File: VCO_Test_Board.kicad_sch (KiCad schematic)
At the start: 19 parts, among them J1 PCB.SMAFRA.HT, J2 PCB.SMAFRA.HT, J3 Tune Voltage Input, J4 VCC, Y1 MAX2607EUT+T

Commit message: Export gerber files.
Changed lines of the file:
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@@
   (junction (at 177.8 88.9) (diameter 0) (color 0 0 0 0)
   )
+  (junction (at 158.75 118.11) (diameter 0) (color 0 0 0 0)
+  )
+  (junction (at 135.89 59.69) (diameter 0) (color 0 0 0 0)
+  )
   (junction (at 175.26 88.9) (diameter 0) (color 0 0 0 0)
   )
@@
   (junction (at 130.81 88.9) (diameter 0) (color 0 0 0 0)
   )
+  (junction (at 147.32 64.77) (diameter 0) (color 0 0 0 0)
+  )
   (junction (at 130.81 86.36) (diameter 0) (color 0 0 0 0)
   )
-  (junction (at 162.56 118.11) (diameter 0) (color 0 0 0 0)
-  )
-  (junction (at 132.08 59.69) (diameter 0) (color 0 0 0 0)
+  (junction (at 135.89 120.65) (diameter 0) (color 0 0 0 0)
   )
   (junction (at 138.43 78.74) (diameter 0) (color 0 0 0 0)
@@
   (junction (at 170.18 91.44) (diameter 0) (color 0 0 0 0)
   )
-  (junction (at 147.32 129.54) (diameter 0) (color 0 0 0 0)
-  )
-  (junction (at 132.08 120.65) (diameter 0) (color 0 0 0 0)
-  )
   (junction (at 138.43 86.36) (diameter 0) (color 0 0 0 0)
   )
-  (junction (at 162.56 57.15) (diameter 0) (color 0 0 0 0)
+  (junction (at 147.32 125.73) (diameter 0) (color 0 0 0 0)
+  )
+  (junction (at 158.75 57.15) (diameter 0) (color 0 0 0 0)
   )
   (junction (at 167.64 86.36) (diameter 0) (color 0 0 0 0)
@@
   (junction (at 119.38 88.9) (diameter 0) (color 0 0 0 0)
   )
-  (junction (at 147.32 68.58) (diameter 0) (color 0 0 0 0)
-  )
   (junction (at 96.52 88.9) (diameter 0) (color 0 0 0 0)
   )
@@
     (stroke (width 0) (type default))
   )
-  (wire (pts (xy 132.08 120.65) (xy 137.16 120.65))
-    (stroke (width 0) (type default))
-  )
-  (wire (pts (xy 147.32 68.58) (xy 162.56 68.58))
+  (wire (pts (xy 147.32 64.77) (xy 158.75 64.77))
     (stroke (width 0) (type default))
   )
@@
     (stroke (width 0) (type default))
   )
-  (wire (pts (xy 132.08 118.11) (xy 137.16 118.11))
+  (wire (pts (xy 135.89 118.11) (xy 137.16 118.11))
     (stroke (width 0) (type default))
   )
@@
     (stroke (width 0) (type default))
   )
-  (wire (pts (xy 157.48 54.61) (xy 162.56 54.61))
+  (wire (pts (xy 147.32 125.73) (xy 147.32 127))
+    (stroke (width 0) (type default))
+  )
+  (wire (pts (xy 157.48 54.61) (xy 158.75 54.61))
     (stroke (width 0) (type default))
   )
@@
     (stroke (width 0) (type default))
   )
-  (wire (pts (xy 147.32 134.62) (xy 147.32 129.54))
-    (stroke (width 0) (type default))
-  )
   (wire (pts (xy 115.57 88.9) (xy 119.38 88.9))
     (stroke (width 0) (type default))
@@
     (stroke (width 0) (type default))
   )
-  (wire (pts (xy 157.48 57.15) (xy 162.56 57.15))
+  (wire (pts (xy 157.48 57.15) (xy 158.75 57.15))
     (stroke (width 0) (type default))
   )
@@
     (stroke (width 0) (type default))
   )
-  (wire (pts (xy 132.08 129.54) (xy 147.32 129.54))
+  (wire (pts (xy 135.89 125.73) (xy 147.32 125.73))
     (stroke (width 0) (type default))
   )
@@
     (stroke (width 0) (type default))
   )
-  (wire (pts (xy 157.48 115.57) (xy 162.56 115.57))
-    (stroke (width 0) (type default))
-  )
-  (wire (pts (xy 132.08 59.69) (xy 137.16 59.69))
-    (stroke (width 0) (type default))
-  )
-  (wire (pts (xy 132.08 120.65) (xy 132.08 118.11))
-    (stroke (width 0) (type default))
-  )
-  (wire (pts (xy 162.56 57.15) (xy 162.56 68.58))
+  (wire (pts (xy 157.48 115.57) (xy 158.75 115.57))
+    (stroke (width 0) (type default))
+  )
+  (wire (pts (xy 135.89 120.65) (xy 135.89 118.11))
+    (stroke (width 0) (type default))
+  )
+  (wire (pts (xy 158.75 57.15) (xy 158.75 64.77))
     (stroke (width 0) (type default))
   )
@@
     (stroke (width 0) (type default))
   )
-  (wire (pts (xy 147.32 69.85) (xy 147.32 68.58))
-    (stroke (width 0) (type default))
-  )
   (wire (pts (xy 175.26 86.36) (xy 175.26 88.9))
     (stroke (width 0) (type default))
   )
-  (wire (pts (xy 162.56 54.61) (xy 162.56 57.15))
-    (stroke (width 0) (type default))
-  )
-  (wire (pts (xy 162.56 115.57) (xy 162.56 118.11))
+  (wire (pts (xy 158.75 54.61) (xy 158.75 57.15))
+    (stroke (width 0) (type default))
+  )
+  (wire (pts (xy 158.75 115.57) (xy 158.75 118.11))
     (stroke (width 0) (type default))
   )
@@
     (stroke (width 0) (type default))
   )
-  (wire (pts (xy 132.08 129.54) (xy 132.08 120.65))
-    (stroke (width 0) (type default))
-  )
-  (wire (pts (xy 132.08 59.69) (xy 132.08 57.15))
-    (stroke (width 0) (type default))
-  )
-  (wire (pts (xy 132.08 57.15) (xy 137.16 57.15))
-    (stroke (width 0) (type default))
-  )
-  (wire (pts (xy 157.48 118.11) (xy 162.56 118.11))
-    (stroke (width 0) (type default))
-  )
-  (wire (pts (xy 132.08 68.58) (xy 147.32 68.58))
-    (stroke (width 0) (type default))
-  )
-  (wire (pts (xy 162.56 118.11) (xy 162.56 129.54))
+  (wire (pts (xy 147.32 64.77) (xy 147.32 66.04))
+    (stroke (width 0) (type default))
+  )
+  (wire (pts (xy 135.89 125.73) (xy 135.89 120.65))
+    (stroke (width 0) (type default))
+  )
+  (wire (pts (xy 135.89 59.69) (xy 135.89 57.15))
+    (stroke (width 0) (type default))
+  )
+  (wire (pts (xy 135.89 57.15) (xy 137.16 57.15))
+    (stroke (width 0) (type default))
+  )
+  (wire (pts (xy 157.48 118.11) (xy 158.75 118.11))
+    (stroke (width 0) (type default))
+  )
+  (wire (pts (xy 135.89 59.69) (xy 137.16 59.69))
+    (stroke (width 0) (type default))
+  )
+  (wire (pts (xy 135.89 120.65) (xy 137.16 120.65))
+    (stroke (width 0) (type default))
+  )
+  (wire (pts (xy 135.89 64.77) (xy 147.32 64.77))
+    (stroke (width 0) (type default))
+  )
+  (wire (pts (xy 158.75 118.11) (xy 158.75 125.73))
     (stroke (width 0) (type default))
   )
@@
     (stroke (width 0) (type default))
   )
-  (wire (pts (xy 147.32 129.54) (xy 162.56 129.54))
+  (wire (pts (xy 147.32 125.73) (xy 158.75 125.73))
     (stroke (width 0) (type default))
   )
@@
     (stroke (width 0) (type default))
   )
-  (wire (pts (xy 132.08 68.58) (xy 132.08 59.69))
+  (wire (pts (xy 135.89 64.77) (xy 135.89 59.69))
     (stroke (width 0) (type default))
   )
@@
     )
   )
-  (symbol (lib_id "power:GND") (at 147.32 134.62 0) (unit 1)
+  (symbol (lib_id "power:GND") (at 147.32 127 0) (unit 1)
     (in_bom yes) (on_board yes) (dnp no) (fields_autoplaced)
-    (property "Reference" "#PWR04" (at 147.32 140.97 0)
-      (effects (font (size 1.27 1.27)) hide)
-    )
-    (property "Value" "GND" (at 147.32 139.7 0)
-      (effects (font (size 1.27 1.27)))
-    )
-    (property "Footprint" "" (at 147.32 134.62 0)
-      (effects (font (size 1.27 1.27)) hide)
-    )
-    (property "Datasheet" "" (at 147.32 134.62 0)
+    (property "Reference" "#PWR04" (at 147.32 133.35 0)
+      (effects (font (size 1.27 1.27)) hide)
+    )
+    (property "Value" "GND" (at 147.32 132.08 0)
+      (effects (font (size 1.27 1.27)))
+    )
+    (property "Footprint" "" (at 147.32 127 0)
+      (effects (font (size 1.27 1.27)) hide)
+    )
+    (property "Datasheet" "" (at 147.32 127 0)
       (effects (font (size 1.27 1.27)) hide)
     )
@@
     )
   )
-  (symbol (lib_id "power:GND") (at 147.32 69.85 0) (unit 1)
+  (symbol (lib_id "power:GND") (at 147.32 66.04 0) (unit 1)
     (in_bom yes) (on_board yes) (dnp no) (fields_autoplaced)
-    (property "Reference" "#PWR03" (at 147.32 76.2 0)
-      (effects (font (size 1.27 1.27)) hide)
-    )
-    (property "Value" "GND" (at 147.32 74.93 0)
-      (effects (font (size 1.27 1.27)))
-    )
-    (property "Footprint" "" (at 147.32 69.85 0)
-      (effects (font (size 1.27 1.27)) hide)
-    )
-    (property "Datasheet" "" (at 147.32 69.85 0)
-      (effects (font (size 1.27 1.27)) hide)
-    )
+    (property "Reference" "#PWR03" (at 147.32 72.39 0)
+      (effects (font (size 1.27 1.27)) hide)
+    )
+    (property "Value" "GND" (at 147.32 71.12 0)
+      (effects (font (size 1.27 1.27)))
+    )
+    (property "Footprint" "" (at 147.32 66.04 0)
+      (effects (font (size 1.27 1.27)) hide)
+    )
+    (property "Datasheet" "" (at 147.32 66.04 0)
+      (effects (font (size 1.27 1.27)) hide)
+    )

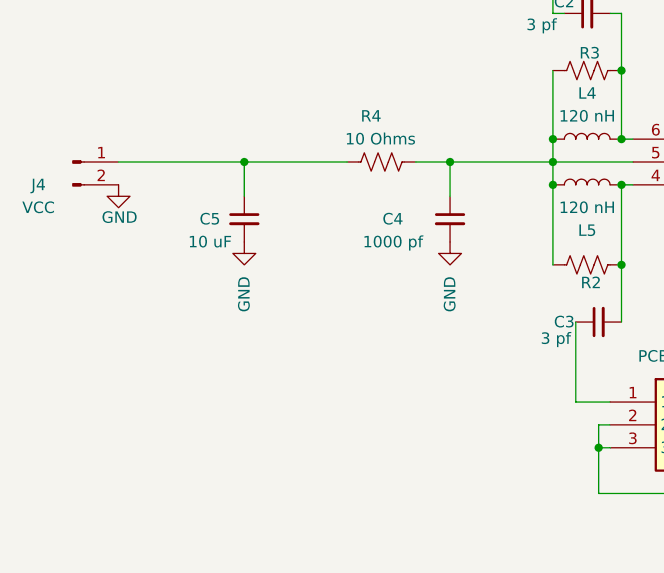
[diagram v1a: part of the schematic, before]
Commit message: Swap out C5 for Tantalum capacitor. Final export for board order.
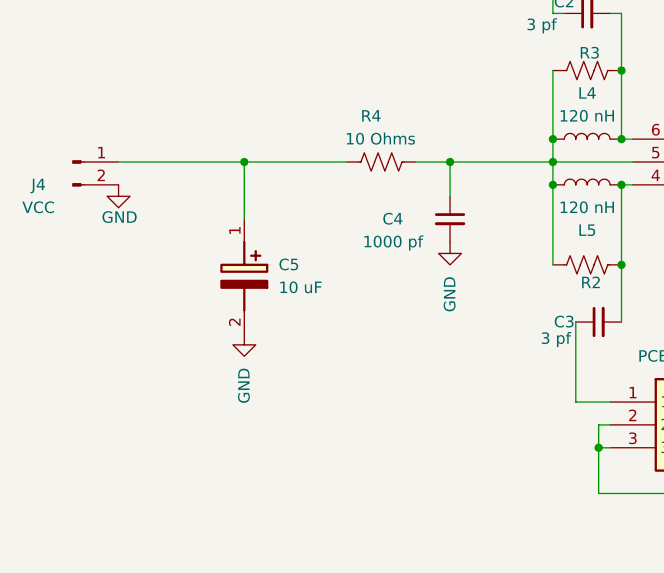
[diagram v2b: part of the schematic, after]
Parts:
- removed C5: 10 uF, Capacitor_SMD:C_1206_3216Metric, symbol Device:C_Small
- added C5: 10 uF, CAPPM6032X280N, symbol Mouser:TAJC106K016RNJ
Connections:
- net GND: now also C5.2 (-)
- net at J4.1 (Pin_1), R4.1: now also C5.1 (+)
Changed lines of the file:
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@@
     (stroke (width 0) (type default))
   )
-  (wire (pts (xy 96.52 92.71) (xy 96.52 88.9))
+  (wire (pts (xy 96.52 95.25) (xy 96.52 88.9))
     (stroke (width 0) (type default))
   )
@@
     )
   )
-  (symbol (lib_id "power:GND") (at 96.52 97.79 0) (mirror y) (unit 1)
-    (in_bom yes) (on_board yes) (dnp no)
-    (property "Reference" "#PWR08" (at 96.52 104.14 0)
-      (effects (font (size 1.27 1.27)) hide)
-    )
-    (property "Value" "GND" (at 96.52 101.6 90)
+  (symbol (lib_id "power:GND") (at 96.52 107.95 0) (mirror y) (unit 1)
+    (in_bom yes) (on_board yes) (dnp no)
+    (property "Reference" "#PWR08" (at 96.52 114.3 0)
+      (effects (font (size 1.27 1.27)) hide)
+    )
+    (property "Value" "GND" (at 96.52 111.76 90)
       (effects (font (size 1.27 1.27)) (justify right))
     )
-    (property "Footprint" "" (at 96.52 97.79 0)
-      (effects (font (size 1.27 1.27)) hide)
-    )
-    (property "Datasheet" "" (at 96.52 97.79 0)
+    (property "Footprint" "" (at 96.52 107.95 0)
+      (effects (font (size 1.27 1.27)) hide)
+    )
+    (property "Datasheet" "" (at 96.52 107.95 0)
       (effects (font (size 1.27 1.27)) hide)
     )
@@
     )
   )
+  (symbol (lib_id "Mouser:TAJC106K016RNJ") (at 96.52 95.25 270) (unit 1)
+    (in_bom yes) (on_board yes) (dnp no) (fields_autoplaced)
+    (property "Reference" "C5" (at 100.33 100.33 90)
+      (effects (font (size 1.27 1.27)) (justify left))
+    )
+    (property "Value" "10 uF" (at 100.33 102.87 90)
+      (effects (font (size 1.27 1.27)) (justify left))
+    )
+    (property "Footprint" "CAPPM6032X280N" (at 0.33 104.14 0)
+      (effects (font (size 1.27 1.27)) (justify left top) hide)
+    )
+    (property "Datasheet" "http://datasheets.avx.com/TAJ.pdf" (at -99.67 104.14 0)
+      (effects (font (size 1.27 1.27)) (justify left top) hide)
+    )
+    (property "Height" "2.8" (at -299.67 104.14 0)
+      (effects (font (size 1.27 1.27)) (justify left top) hide)
+    )
+    (property "Mouser Part Number" "581-TAJC106K016" (at -399.67 104.14 0)
+      (effects (font (size 1.27 1.27)) (justify left top) hide)
+    )
+    (property "Mouser Price/Stock" "https://www.mouser.co.uk/ProductDetail/AVX/TAJC106K016RNJ?qs=ZjRtS80k2UPxdN5lyYHtCw%3D%3D" (at -499.67 104.14 0)
+      (effects (font (size 1.27 1.27)) (justify left top) hide)
+    )
+    (property "Manufacturer_Name" "AVX" (at -599.67 104.14 0)
+      (effects (font (size 1.27 1.27)) (justify left top) hide)
+    )
+    (property "Manufacturer_Part_Number" "TAJC106K016RNJ" (at -699.67 104.14 0)
+      (effects (font (size 1.27 1.27)) (justify left top) hide)
+    )
+    (pin "1")
+    (pin "2")
+    (instances
+      (project "VCO_Test_Board"
+        (path "/8d56cd3a-b5ae-4a77-84ce-bb53bc253f71"
+          (reference "C5") (unit 1)
+        )
+      )
+    )
+  )
   (symbol (lib_id "Device:L") (at 171.45 86.36 90) (unit 1)
     (in_bom yes) (on_board yes) (dnp no) (fields_autoplaced)
@@
         )
       )
-    )
-  )
-  (symbol (lib_id "Device:C_Small") (at 96.52 95.25 0) (unit 1)
-    (in_bom yes) (on_board yes) (dnp no)
-    (property "Reference" "C5" (at 92.71 95.25 0)
-      (effects (font (size 1.27 1.27)))
-    )
-    (property "Value" "10 uF" (at 92.71 97.79 0)
-      (effects (font (size 1.27 1.27)))
-    )
-    (property "Footprint" "Capacitor_SMD:C_1206_3216Metric" (at 96.52 95.25 0)
-      (effects (font (size 1.27 1.27)) hide)
-    )
-    (property "Datasheet" "~" (at 96.52 95.25 0)
-      (effects (font (size 1.27 1.27)) hide)
-    )
-    (pin "1")
-    (pin "2")
-    (instances
-      (project "VCO_Test_Board"
-        (path "/8d56cd3a-b5ae-4a77-84ce-bb53bc253f71"
-          (reference "C5") (unit 1)
-        )
-      )
-      (project "UpDownConverter"
-        (path "/cc9fcf9b-b84f-49ca-8b98-f0ff7034b4a0"
-          (reference "C2") (unit 1)
-        )
-        (path "/cc9fcf9b-b84f-49ca-8b98-f0ff7034b4a0/b126e69a-9c0d-4c01-8f3e-221dd78a02d4"
-          (reference "C2") (unit 1)
-        )
-        (path "/cc9fcf9b-b84f-49ca-8b98-f0ff7034b4a0/32631ea7-57a7-4016-8f88-d0d0383e4511"
-          (reference "C41") (unit 1)
-        )
-      )
